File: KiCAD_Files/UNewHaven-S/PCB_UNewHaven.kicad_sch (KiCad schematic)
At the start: 23 parts, among them J1 Conn_01x15_Female, J2 Conn_01x15_Female, SW1 SW_Push, SW2 SW_Push, SW3 SW_Push, U2 LM35-LP

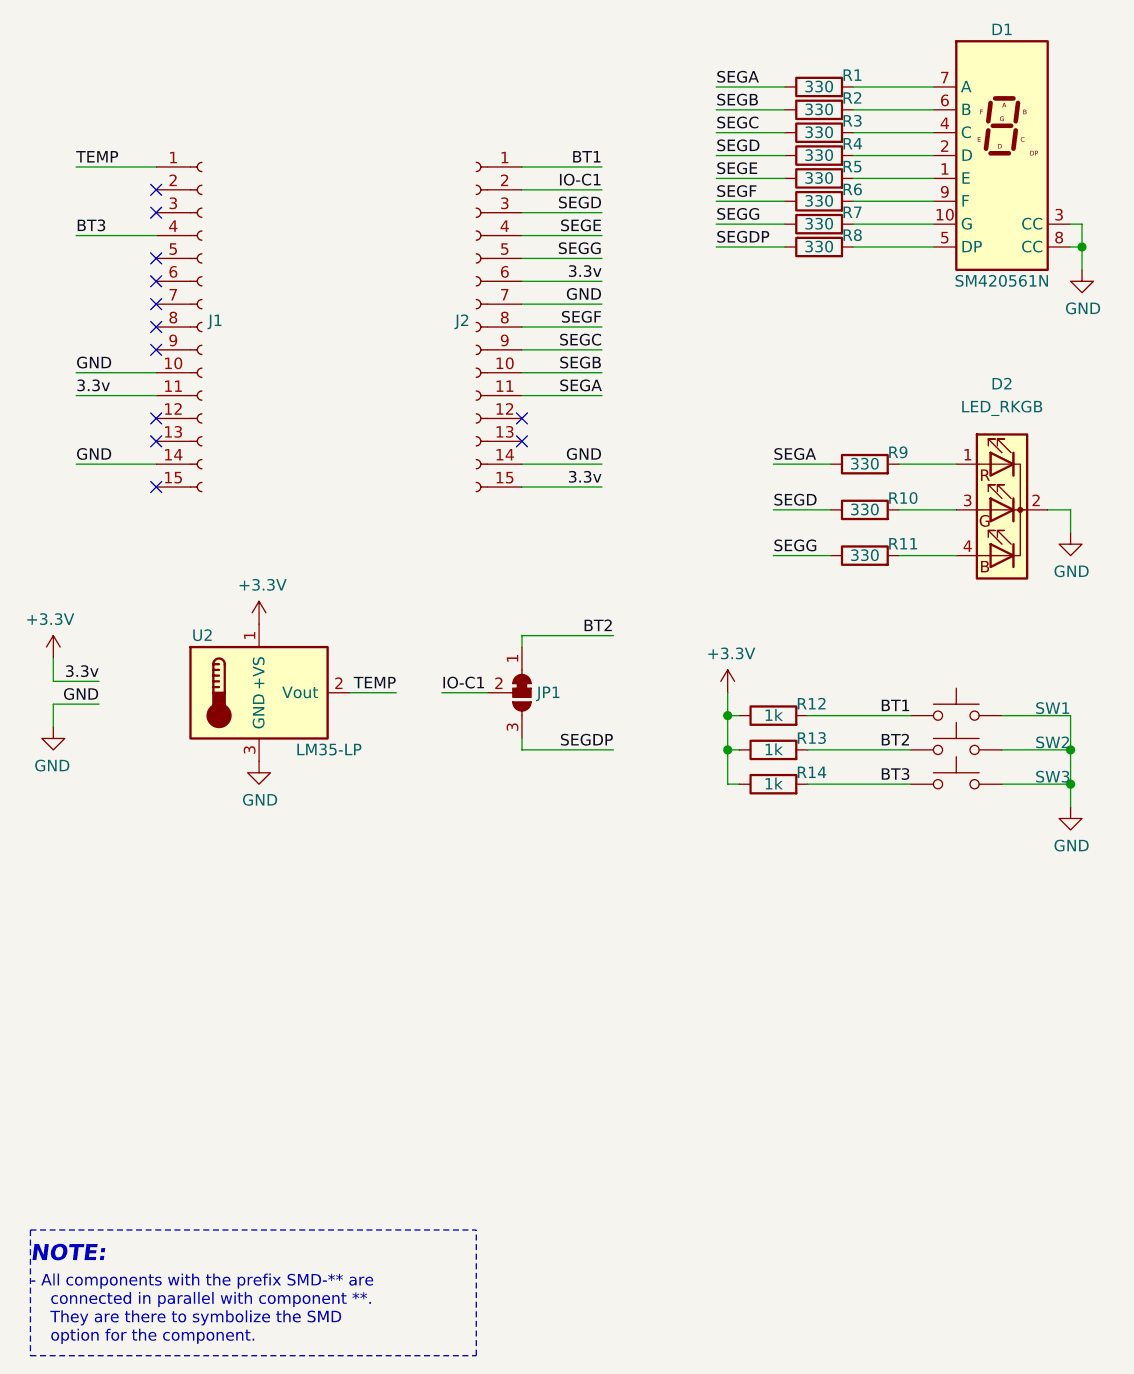
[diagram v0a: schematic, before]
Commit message: UNewHaven Version 1.2 Update. Removed project from pre-release in README.md
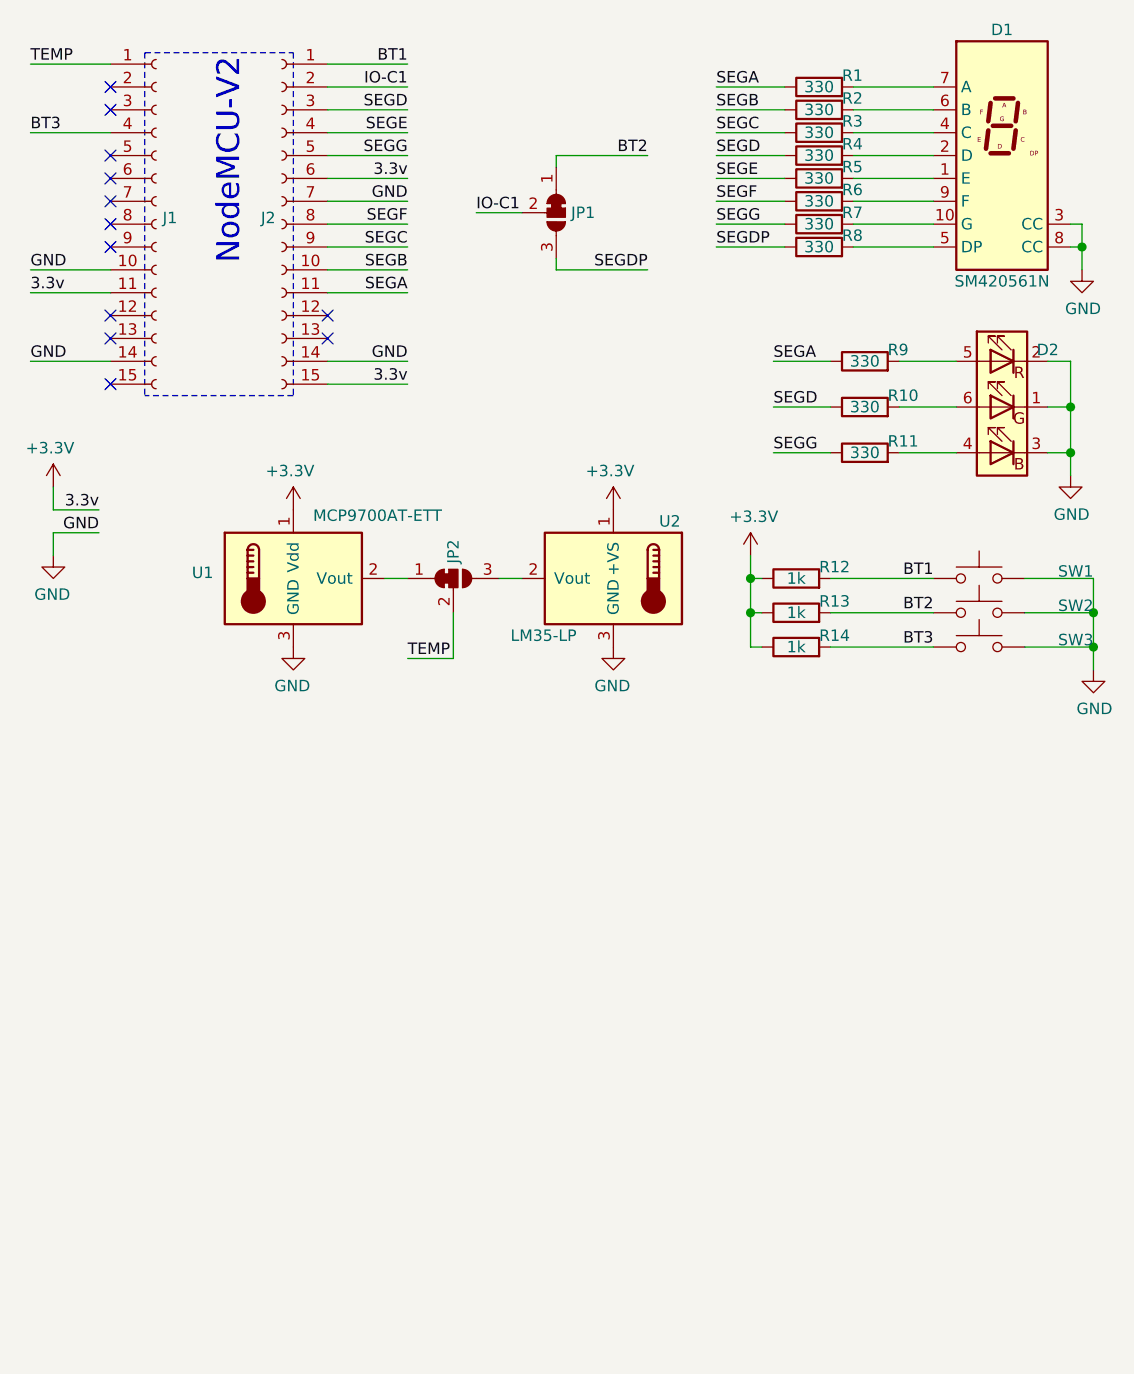
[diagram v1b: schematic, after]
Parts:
- removed D2: LED_RKGB, LED_THT:LED_D5.0mm-4_RGB_Staggered_Pins, symbol Device:LED_RKGB
- added D2: LED_RGB, LED_SMD:LED_RGB_5050-6, symbol Device:LED_RGB
- added JP2: SolderJumper_3_Bridged12, Jumper:SolderJumper-3_P1.3mm_Bridged12_Pad1.0x1.5mm, symbol Jumper:SolderJumper_3_Bridged12
- added U1: MCP9700AT-ETT, Package_TO_SOT_SMD:SOT-23, symbol Sensor_Temperature:MCP9700AT-ETT
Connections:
- net +3V3: now also U1.1 (Vdd)
- net GND: now also D2.1 (GK), D2.2 (RK), D2.3 (BK), U1.3 (GND)
- net TEMP: now also JP2.2 (C); no longer U2.2 (Vout)
- net at R11.2: now also D2.4 (BA)
- net at R9.2: now also D2.5 (RA)
- net at R10.2: now also D2.6 (GA)
- new net: JP2.1 (A), U1.2 (Vout)
- new net: JP2.3 (B), U2.2 (Vout)
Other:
- note added: "NodeMCU-V2"
- note removed: "- All components with the prefix SMD-** are connected in parallel with component **. They are there to symbolize the SMD option for the component."
- note removed: "NOTE:"
- moved on the sheet: J1, J2, JP1, R10, R11, R12, R13, R14, R9, SW1, SW2, SW3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

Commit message: Almost finished Rev1.3 of the UNewHaven board
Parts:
- added BZ1: Buzzer, Buzzer_Beeper:Buzzer_12x9.5RM7.6, symbol Device:Buzzer
- added R15: 1k, Resistor_SMD:R_1206_3216Metric_Pad1.30x1.75mm_HandSolder, symbol Device:R
- added SW-T1, SW-T2, SW-T3: SW_Push_DPDT, Button_Switch_THT:SW_CuK_JS202011CQN_DPDT_Straight, symbol Switch:SW_Push_DPDT
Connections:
- net BT1: now also SW-T1.2 (B), SW-T1.5 (B)
- net BT2: now also SW-T2.2 (B), SW-T2.5 (B)
- net BT3: now also SW-T3.2 (B), SW-T3.5 (B)
- net GND: now also BZ1.2 (+), SW-T1.1 (A), SW-T1.4 (A), SW-T2.1 (A), SW-T2.4 (A), SW-T3.1 (A), SW-T3.4 (A)
- net SEGDP: now also R15.2
- new net: BZ1.1 (-), R15.1

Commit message: Added some external pin headers
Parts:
- added J3, J4, J5, J6: Conn_01x01_Female, CustomFootprints:SingleExternalWire, symbol Connector:Conn_01x01_Female
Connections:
- net GND: now also J4.1 (Pin_1)
- net IO-C1: now also J5.1 (Pin_1)
- net TEMP: now also J6.1 (Pin_1)
- net VIN: now reaches J1.15 (Pin_15)
- net VIN: now also J3.1 (Pin_1)
- no-connect marks 12 -> 11

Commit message: Changed the external pinout's connectors. Minor silk changes. DRC fixes
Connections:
- net SEGG: now also J6.1 (Pin_1)
- net TEMP: no longer J6.1 (Pin_1)
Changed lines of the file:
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@@
     (effects (font (size 2.54 2.54)) (justify right bottom))
-  )
-  (label "TEMP" (at 17.78 128.27 0)
-    (effects (font (size 1.27 1.27)) (justify left bottom))
   )
   (label "VIN" (at 17.78 120.65 0)
@@
     (effects (font (size 1.27 1.27)) (justify left bottom))
   )
-  (label "IO-C1" (at 17.78 125.73 0)
-    (effects (font (size 1.27 1.27)) (justify left bottom))
-  )
   (label "BT1" (at 115.57 76.2 180)
     (effects (font (size 1.27 1.27)) (justify right bottom))
@@
     (effects (font (size 1.27 1.27)) (justify left bottom))
   )
+  (label "IO-C1" (at 17.78 125.73 0)
+    (effects (font (size 1.27 1.27)) (justify left bottom))
+  )
   (label "SEGDP" (at 91.44 39.37 0)
     (effects (font (size 1.27 1.27)) (justify left bottom))
   )
+  (label "SEGG" (at 17.78 128.27 0)
+    (effects (font (size 1.27 1.27)) (justify left bottom))
+  )

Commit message: Added LCSC component attributes
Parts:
- D1: LCSC (none) -> C141367
- J1, J2: LCSC (none) -> C124408
- J3, J4, J5, J6: now left out of the parts list
- R1, R10, R11, R2, R3, R4, R5, R6, R7, R8, R9: LCSC (none) -> C17930
- R12, R13, R14: LCSC (none) -> C4410
- SW-T1, SW-T2, SW-T3: LCSC (none) -> C221666
- SW1, SW2, SW3: LCSC (none) -> C136669
- U1: LCSC (none) -> C127949
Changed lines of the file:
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@@
       (effects (font (size 1.27 1.27)) (justify left) hide)
+    )
+    (property "LCSC" "C141367" (id 4) (at 123.19 29.21 0)
+      (effects (font (size 1.27 1.27)) hide)
     )
     (pin "1")
@@
       (effects (font (size 1.27 1.27)) hide)
     )
+    (property "LCSC" "C17930" (id 4) (at 107.95 62.23 90)
+      (effects (font (size 1.27 1.27)) hide)
+    )
     (pin "1")
     (pin "2")
@@
       (effects (font (size 1.27 1.27)) hide)
     )
+    (property "LCSC" "C17930" (id 4) (at 102.87 21.59 90)
+      (effects (font (size 1.27 1.27)) hide)
+    )
     (pin "1")
     (pin "2")
   )
   (symbol (lib_id "Connector:Conn_01x01_Female") (at 30.48 123.19 0) (unit 1)
-    (in_bom yes) (on_board yes)
+    (in_bom no) (on_board yes)
     (property "Reference" "J4" (id 0) (at 31.75 123.19 0)
       (effects (font (size 1.27 1.27)) (justify left))
@@
     )
     (property "Datasheet" "~" (id 3) (at 43.18 36.83 0)
+      (effects (font (size 1.27 1.27)) hide)
+    )
+    (property "LCSC" "C124408" (id 4) (at 43.18 36.83 0)
       (effects (font (size 1.27 1.27)) hide)
     )
@@
       (effects (font (size 1.27 1.27)) hide)
     )
+    (property "LCSC" "C221666" (id 4) (at 125.73 99.06 0)
+      (effects (font (size 1.27 1.27)) hide)
+    )
     (pin "1")
     (pin "2")
@@
       (effects (font (size 1.27 1.27)) hide)
     )
+    (property "LCSC" "C4410" (id 4) (at 100.33 83.82 90)
+      (effects (font (size 1.27 1.27)) hide)
+    )
     (pin "1")
     (pin "2")
@@
       (effects (font (size 1.27 1.27)) hide)
     )
+    (property "LCSC" "C17930" (id 4) (at 102.87 34.29 90)
+      (effects (font (size 1.27 1.27)) hide)
+    )
     (pin "1")
     (pin "2")
@@
       (effects (font (size 1.27 1.27)) hide)
     )
+    (property "LCSC" "C4410" (id 4) (at 100.33 76.2 90)
+      (effects (font (size 1.27 1.27)) hide)
+    )
     (pin "1")
     (pin "2")
@@
       (effects (font (size 1.27 1.27)) hide)
     )
+    (property "LCSC" "C136669" (id 4) (at 120.65 76.2 0)
+      (effects (font (size 1.27 1.27)) hide)
+    )
     (pin "1")
     (pin "2")
@@
   )
   (symbol (lib_id "Connector:Conn_01x01_Female") (at 30.48 125.73 0) (unit 1)
-    (in_bom yes) (on_board yes)
+    (in_bom no) (on_board yes)
     (property "Reference" "J5" (id 0) (at 31.75 125.73 0)
       (effects (font (size 1.27 1.27)) (justify left))
@@
       (effects (font (size 1.27 1.27)) hide)
     )
+    (property "LCSC" "C17930" (id 4) (at 102.87 36.83 90)
+      (effects (font (size 1.27 1.27)) hide)
+    )
     (pin "1")
     (pin "2")
@@
     )
     (property "Datasheet" "~" (id 3) (at 107.95 93.98 0)
+      (effects (font (size 1.27 1.27)) hide)
+    )
+    (property "LCSC" "C221666" (id 4) (at 107.95 99.06 0)
       (effects (font (size 1.27 1.27)) hide)
     )
@@
       (effects (font (size 1.27 1.27)) hide)
     )
+    (property "LCSC" "C136669" (id 4) (at 120.65 83.82 0)
+      (effects (font (size 1.27 1.27)) hide)
+    )
     (pin "1")
     (pin "2")
@@
       (effects (font (size 1.27 1.27)) hide)
     )
+    (property "LCSC" "C17930" (id 4) (at 102.87 31.75 90)
+      (effects (font (size 1.27 1.27)) hide)
+    )
     (pin "1")
     (pin "2")
@@
       (effects (font (size 1.27 1.27)) hide)
     )
+    (property "LCSC" "C136669" (id 4) (at 120.65 80.01 0)
+      (effects (font (size 1.27 1.27)) hide)
+    )
     (pin "1")
     (pin "2")
@@
       (effects (font (size 1.27 1.27)) hide)
     )
+    (property "LCSC" "C17930" (id 4) (at 107.95 52.07 90)
+      (effects (font (size 1.27 1.27)) hide)
+    )
     (pin "1")
     (pin "2")
@@
       (effects (font (size 1.27 1.27)) hide)
     )
+    (property "LCSC" "C17930" (id 4) (at 102.87 39.37 90)
+      (effects (font (size 1.27 1.27)) hide)
+    )
     (pin "1")
     (pin "2")
@@
     )
     (property "Datasheet" "http://ww1.microchip.com/downloads/en/DeviceDoc/21942e.pdf" (id 3) (at 40.64 69.85 0)
+      (effects (font (size 1.27 1.27)) hide)
+    )
+    (property "LCSC" "C127949" (id 4) (at 44.45 76.2 0)
       (effects (font (size 1.27 1.27)) hide)
     )
@@
       (effects (font (size 1.27 1.27)) hide)
     )
+    (property "LCSC" "C17930" (id 4) (at 102.87 26.67 90)
+      (effects (font (size 1.27 1.27)) hide)
+    )
     (pin "1")
     (pin "2")
@@
       (effects (font (size 1.27 1.27)) hide)
     )
+    (property "LCSC" "C4410" (id 4) (at 100.33 80.01 90)
+      (effects (font (size 1.27 1.27)) hide)
+    )
     (pin "1")
     (pin "2")
@@
       (effects (font (size 1.27 1.27)) hide)
     )
+    (property "LCSC" "C17930" (id 4) (at 102.87 24.13 90)
+      (effects (font (size 1.27 1.27)) hide)
+    )
     (pin "1")
     (pin "2")
@@
   )
   (symbol (lib_id "Connector:Conn_01x01_Female") (at 30.48 128.27 0) (unit 1)
-    (in_bom yes) (on_board yes)
+    (in_bom no) (on_board yes)
     (property "Reference" "J6" (id 0) (at 31.75 128.27 0)
       (effects (font (size 1.27 1.27)) (justify left))
@@
       (effects (font (size 1.27 1.27)) hide)
     )
+    (property "LCSC" "C17930" (id 4) (at 107.95 57.15 90)
+      (effects (font (size 1.27 1.27)) hide)
+    )
     (pin "1")
     (pin "2")
@@
       (effects (font (size 1.27 1.27)) hide)
     )
+    (property "LCSC" "C17930" (id 4) (at 102.87 29.21 90)
+      (effects (font (size 1.27 1.27)) hide)
+    )
     (pin "1")
     (pin "2")
   )
   (symbol (lib_id "Connector:Conn_01x01_Female") (at 30.48 120.65 0) (unit 1)
-    (in_bom yes) (on_board yes)
+    (in_bom no) (on_board yes)
     (property "Reference" "J3" (id 0) (at 31.75 120.65 0)
       (effects (font (size 1.27 1.27)) (justify left))
@@
     )
     (property "Datasheet" "~" (id 3) (at 29.21 36.83 0)
+      (effects (font (size 1.27 1.27)) hide)
+    )
+    (property "LCSC" "C124408" (id 4) (at 29.21 36.83 0)
       (effects (font (size 1.27 1.27)) hide)
     )
@@
       (effects (font (size 1.27 1.27)) hide)
     )
+    (property "LCSC" "C221666" (id 4) (at 90.17 99.06 0)
+      (effects (font (size 1.27 1.27)) hide)
+    )
